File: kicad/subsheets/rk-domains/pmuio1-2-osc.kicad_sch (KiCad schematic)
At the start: 22 parts, among them U5 RK3566

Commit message: Mark as R1.0
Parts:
- renumbered C141 to C100, C142 to C101, C110 to C102, C131 to C103, C132 to C89, C133 to C90, C119 to C91, C128 to C92, C120 to C93, C139 to C94, C140 to C95, C138 to C96, C147 to C97, C143 to C98, C144 to C99, R50 to R33, R48 to R34, R49 to R35, R31 to R36, R53 to R37
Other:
- company: (none) -> UVic Rocketry

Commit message: Annotations
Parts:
- renumbered C89 to C102, C90 to C103, C91 to C104, C92 to C105, C93 to C106, C94 to C107, C95 to C108, C96 to C109, C97 to C110, C98 to C111, C99 to C112, C100 to C113, C101 to C114, C102 to C115, C103 to C116, R33 to R36, R34 to R37, R35 to R38, R36 to R39, R37 to R40

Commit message: Minor tweaks + annotations
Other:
- moved on the sheet: C102, C103

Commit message: Start on PCB design
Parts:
- C100: renamed from C102; footprint (none) -> Capacitor_SMD:C_0402_1005Metric; LCSC PART NAME (none) -> C1525
- C101: renamed from C103; footprint (none) -> Capacitor_SMD:C_0603_1608Metric; LCSC PART NAME (none) -> C15849
- C102: renamed from C104; value 18pF -> 22pF; footprint (none) -> Capacitor_SMD:C_0402_1005Metric; LCSC PART NAME (none) -> C1555
- C103: renamed from C105; footprint (none) -> Capacitor_SMD:C_0402_1005Metric; LCSC PART NAME (none) -> C1525
- C104: renamed from C106; value 18pF -> 22pF; footprint (none) -> Capacitor_SMD:C_0402_1005Metric; LCSC PART NAME (none) -> C1555
- C105: renamed from C107; footprint (none) -> Capacitor_SMD:C_0603_1608Metric; LCSC PART NAME (none) -> C15849
- C106: renamed from C108; footprint (none) -> Capacitor_SMD:C_0402_1005Metric; LCSC PART NAME (none) -> C1525
- C107: renamed from C109; footprint (none) -> Capacitor_SMD:C_0603_1608Metric; LCSC PART NAME (none) -> C15849
- C108: renamed from C110; footprint (none) -> Capacitor_SMD:C_0402_1005Metric; LCSC PART NAME (none) -> C1525
- C109: renamed from C111; footprint (none) -> Capacitor_SMD:C_0603_1608Metric; LCSC PART NAME (none) -> C15849
- C110: renamed from C112; footprint (none) -> Capacitor_SMD:C_0402_1005Metric; LCSC PART NAME (none) -> C1525
- C111: renamed from C113; footprint (none) -> Capacitor_SMD:C_0603_1608Metric; LCSC PART NAME (none) -> C15849
- C112: renamed from C114; footprint (none) -> Capacitor_SMD:C_0402_1005Metric; LCSC PART NAME (none) -> C1525
- C113: renamed from C115; footprint (none) -> Capacitor_SMD:C_0402_1005Metric; LCSC PART NAME (none) -> C1525
- C114: renamed from C116; footprint (none) -> Capacitor_SMD:C_0402_1005Metric; LCSC PART NAME (none) -> C1525
- HSE2: footprint (none) -> Crystal:Crystal_SMD_2016-4Pin_2.0x1.6mm; LCSC PART NAME (none) -> C725986
- R37: renamed from R36; footprint (none) -> Resistor_SMD:R_0402_1005Metric; LCSC PART NAME (none) -> C25092
- R38: renamed from R37; footprint (none) -> Resistor_SMD:R_0402_1005Metric; LCSC PART NAME (none) -> C17168
- R39: renamed from R38; footprint (none) -> Resistor_SMD:R_0402_1005Metric; LCSC PART NAME (none) -> C26083
- R40: renamed from R39; footprint (none) -> Resistor_SMD:R_0402_1005Metric; LCSC PART NAME (none) -> C17168
- R41: renamed from R40; footprint (none) -> Resistor_SMD:R_0402_1005Metric; LCSC PART NAME (none) -> C25076
- U5: LCSC PART NAME RK3566 -> (none)

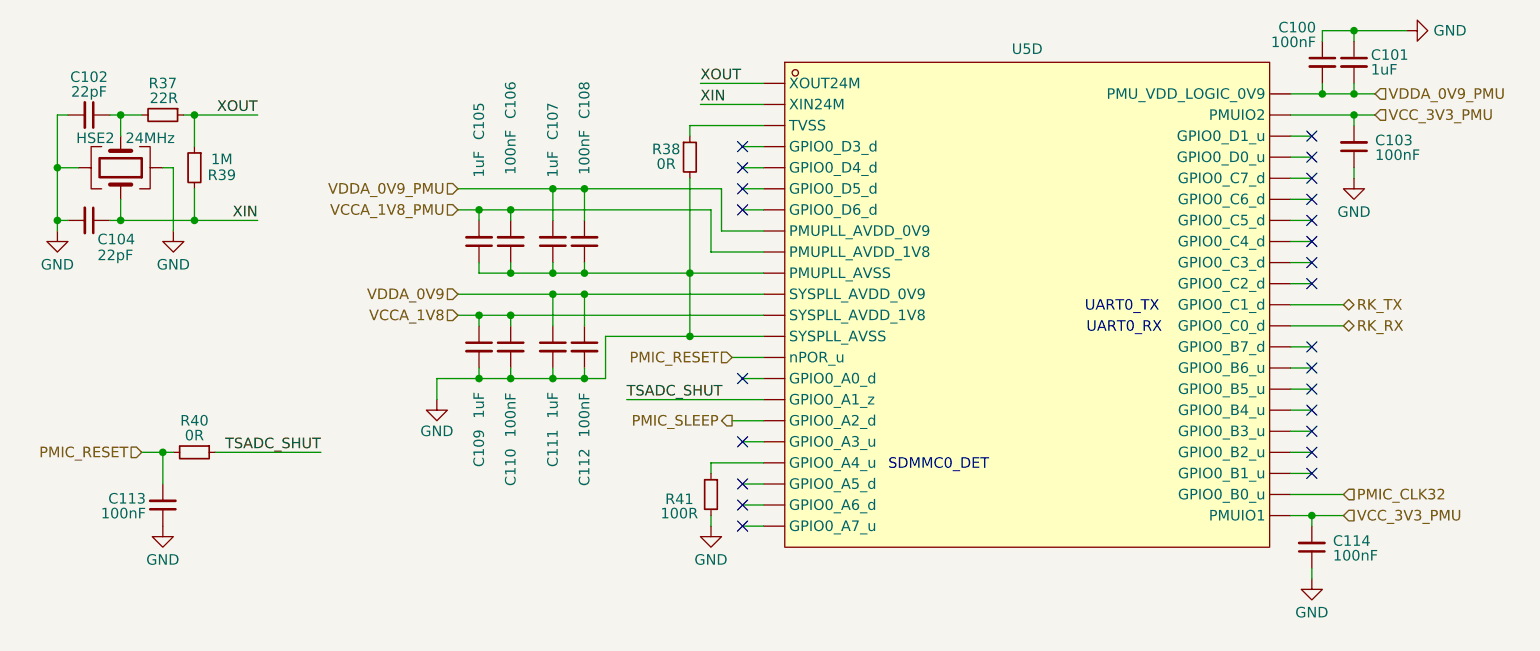
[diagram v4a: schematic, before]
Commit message: Remove power/decoupling for unused power domains
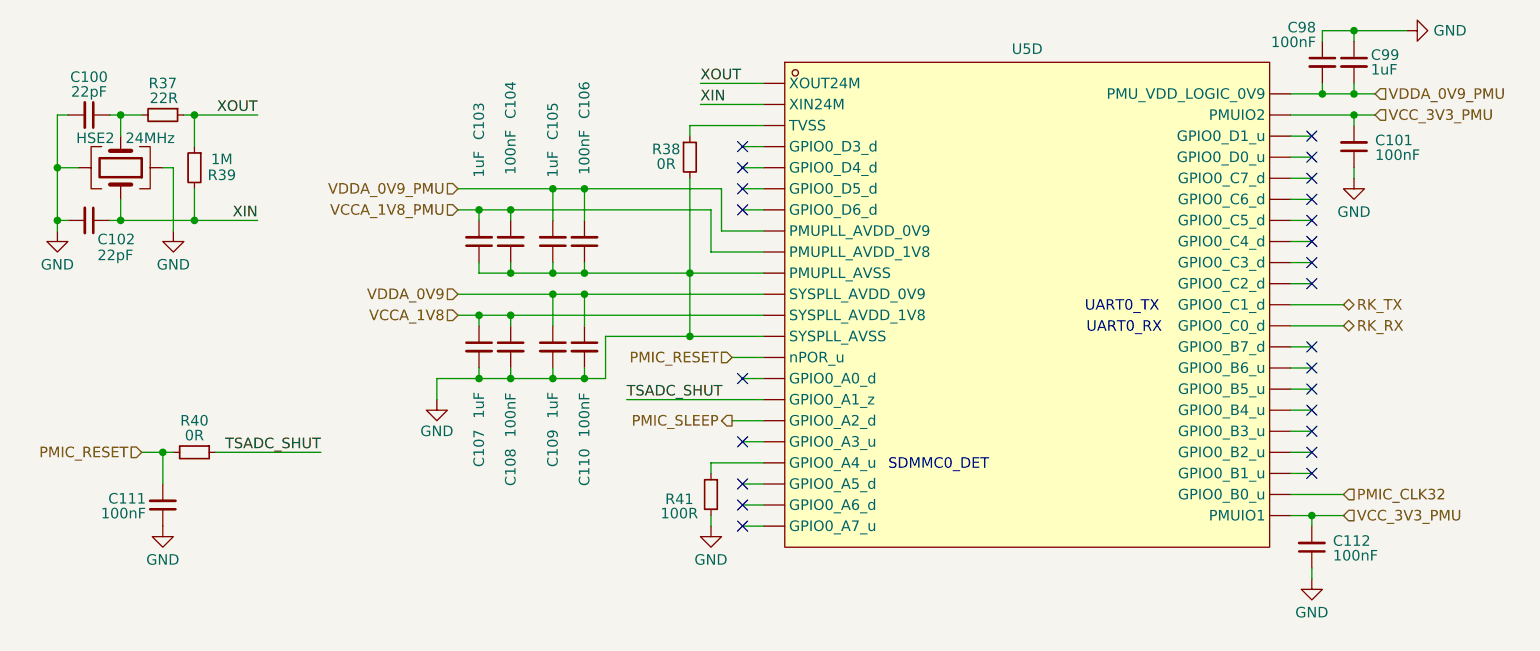
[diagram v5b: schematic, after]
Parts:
- renumbered C102 to C100, C103 to C101, C104 to C102, C105 to C103, C106 to C104, C107 to C105, C108 to C106, C109 to C107, C110 to C108, C111 to C109, C112 to C110, C113 to C111, C114 to C112, C100 to C98, C101 to C99
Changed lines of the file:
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@@
 		(on_board yes)
 		(dnp no)
-		(property "Reference" "C103"
+		(property "Reference" "C101"
 			(at 222.25 76.7145 0)
 			(effects
@@
 			(project "srad-camera"
 				(path "/da62c771-e8c9-451f-8df1-ec995aadcb11/279fc251-45a8-41a3-8fcf-5855d7fe07da/797477a3-3a48-4b27-a4d8-748eafbd5280"
-					(reference "C103")
+					(reference "C101")
 					(unit 1)
 				)
@@
 		(on_board yes)
 		(dnp no)
-		(property "Reference" "C106"
+		(property "Reference" "C104"
 			(at 118.11 69.596 90)
 			(effects
@@
 			(project "srad-camera"
 				(path "/da62c771-e8c9-451f-8df1-ec995aadcb11/279fc251-45a8-41a3-8fcf-5855d7fe07da/797477a3-3a48-4b27-a4d8-748eafbd5280"
-					(reference "C106")
+					(reference "C104")
 					(unit 1)
 				)
@@
 		(on_board yes)
 		(dnp no)
-		(property "Reference" "#PWR079"
+		(property "Reference" "#PWR082"
 			(at 142.24 129.54 0)
 			(effects
@@
 			(project "srad-camera"
 				(path "/da62c771-e8c9-451f-8df1-ec995aadcb11/279fc251-45a8-41a3-8fcf-5855d7fe07da/797477a3-3a48-4b27-a4d8-748eafbd5280"
-					(reference "#PWR079")
+					(reference "#PWR082")
 					(unit 1)
 				)
@@
 		(on_board yes)
 		(dnp no)
-		(property "Reference" "C108"
+		(property "Reference" "C106"
 			(at 127 69.596 90)
 			(effects
@@
 			(project "srad-camera"
 				(path "/da62c771-e8c9-451f-8df1-ec995aadcb11/279fc251-45a8-41a3-8fcf-5855d7fe07da/797477a3-3a48-4b27-a4d8-748eafbd5280"
-					(reference "C108")
+					(reference "C106")
 					(unit 1)
 				)
@@
 		(on_board yes)
 		(dnp no)
-		(property "Reference" "C114"
+		(property "Reference" "C112"
 			(at 217.17 124.9745 0)
 			(effects
@@
 			(project "srad-camera"
 				(path "/da62c771-e8c9-451f-8df1-ec995aadcb11/279fc251-45a8-41a3-8fcf-5855d7fe07da/797477a3-3a48-4b27-a4d8-748eafbd5280"
-					(reference "C114")
+					(reference "C112")
 					(unit 1)
 				)
@@
 		(on_board yes)
 		(dnp no)
-		(property "Reference" "#PWR076"
+		(property "Reference" "#PWR079"
 			(at 77.47 93.98 0)
 			(effects
@@
 			(project "srad-camera"
 				(path "/da62c771-e8c9-451f-8df1-ec995aadcb11/279fc251-45a8-41a3-8fcf-5855d7fe07da/797477a3-3a48-4b27-a4d8-748eafbd5280"
-					(reference "#PWR076")
+					(reference "#PWR079")
 					(unit 1)
 				)
@@
 		(on_board yes)
 		(dnp no)
-		(property "Reference" "C101"
+		(property "Reference" "C99"
 			(at 221.742 66.4275 0)
 			(effects
@@
 			(project "srad-camera"
 				(path "/da62c771-e8c9-451f-8df1-ec995aadcb11/279fc251-45a8-41a3-8fcf-5855d7fe07da/797477a3-3a48-4b27-a4d8-748eafbd5280"
-					(reference "C101")
+					(reference "C99")
 					(unit 1)
 				)
@@
 		(on_board yes)
 		(dnp no)
-		(property "Reference" "C112"
+		(property "Reference" "C110"
 			(at 127 118.364 90)
 			(effects
@@
 			(project "srad-camera"
 				(path "/da62c771-e8c9-451f-8df1-ec995aadcb11/279fc251-45a8-41a3-8fcf-5855d7fe07da/797477a3-3a48-4b27-a4d8-748eafbd5280"
-					(reference "C112")
+					(reference "C110")
 					(unit 1)
 				)
@@
 		(on_board yes)
 		(dnp no)
-		(property "Reference" "#PWR077"
+		(property "Reference" "#PWR080"
 			(at 109.22 114.3 0)
 			(effects
@@
 			(project "srad-camera"
 				(path "/da62c771-e8c9-451f-8df1-ec995aadcb11/279fc251-45a8-41a3-8fcf-5855d7fe07da/797477a3-3a48-4b27-a4d8-748eafbd5280"
-					(reference "#PWR077")
+					(reference "#PWR080")
 					(unit 1)
 				)
@@
 		(on_board yes)
 		(dnp no)
-		(property "Reference" "C107"
+		(property "Reference" "C105"
 			(at 123.19 72.136 90)
 			(effects
@@
 			(project "srad-camera"
 				(path "/da62c771-e8c9-451f-8df1-ec995aadcb11/279fc251-45a8-41a3-8fcf-5855d7fe07da/797477a3-3a48-4b27-a4d8-748eafbd5280"
-					(reference "C107")
+					(reference "C105")
 					(unit 1)
 				)
@@
 		(on_board yes)
 		(dnp no)
-		(property "Reference" "#PWR075"
+		(property "Reference" "#PWR078"
 			(at 63.5 93.98 0)
 			(effects
@@
 			(project "srad-camera"
 				(path "/da62c771-e8c9-451f-8df1-ec995aadcb11/279fc251-45a8-41a3-8fcf-5855d7fe07da/797477a3-3a48-4b27-a4d8-748eafbd5280"
-					(reference "#PWR075")
+					(reference "#PWR078")
 					(unit 1)
 				)
@@
 		(on_board yes)
 		(dnp no)
-		(property "Reference" "C100"
+		(property "Reference" "C98"
 			(at 215.138 63.119 0)
 			(effects
@@
 			(project "srad-camera"
 				(path "/da62c771-e8c9-451f-8df1-ec995aadcb11/279fc251-45a8-41a3-8fcf-5855d7fe07da/797477a3-3a48-4b27-a4d8-748eafbd5280"
-					(reference "C100")
+					(reference "C98")
 					(unit 1)
 				)
@@
 		(dnp no)
 		(fields_autoplaced yes)
-		(property "Reference" "#PWR080"
+		(property "Reference" "#PWR083"
 			(at 214.63 135.89 0)
 			(effects
@@
 			(project "srad-camera"
 				(path "/da62c771-e8c9-451f-8df1-ec995aadcb11/279fc251-45a8-41a3-8fcf-5855d7fe07da/797477a3-3a48-4b27-a4d8-748eafbd5280"
-					(reference "#PWR080")
+					(reference "#PWR083")
 					(unit 1)
 				)
@@
 		(dnp no)
 		(fields_autoplaced yes)
-		(property "Reference" "#PWR074"
+		(property "Reference" "#PWR077"
 			(at 219.71 87.63 0)
 			(effects
@@
 			(project "srad-camera"
 				(path "/da62c771-e8c9-451f-8df1-ec995aadcb11/279fc251-45a8-41a3-8fcf-5855d7fe07da/797477a3-3a48-4b27-a4d8-748eafbd5280"
-					(reference "#PWR074")
+					(reference "#PWR077")
 					(unit 1)
 				)
@@
 		(on_board yes)
 		(dnp no)
-		(property "Reference" "C105"
+		(property "Reference" "C103"
 			(at 114.3 72.136 90)
 			(effects
@@
 			(project "srad-camera"
 				(path "/da62c771-e8c9-451f-8df1-ec995aadcb11/279fc251-45a8-41a3-8fcf-5855d7fe07da/797477a3-3a48-4b27-a4d8-748eafbd5280"
-					(reference "C105")
+					(reference "C103")
 					(unit 1)
 				)
@@
 		(on_board yes)
 		(dnp no)
-		(property "Reference" "C104"
+		(property "Reference" "C102"
 			(at 68.326 88.646 90)
 			(effects
@@
 			(project "srad-camera"
 				(path "/da62c771-e8c9-451f-8df1-ec995aadcb11/279fc251-45a8-41a3-8fcf-5855d7fe07da/797477a3-3a48-4b27-a4d8-748eafbd5280"
-					(reference "C104")
+					(reference "C102")
 					(unit 1)
 				)
@@
 		(on_board yes)
 		(dnp no)
-		(property "Reference" "C110"
+		(property "Reference" "C108"
 			(at 118.11 118.364 90)
 			(effects
@@
 			(project "srad-camera"
 				(path "/da62c771-e8c9-451f-8df1-ec995aadcb11/279fc251-45a8-41a3-8fcf-5855d7fe07da/797477a3-3a48-4b27-a4d8-748eafbd5280"
-					(reference "C110")
+					(reference "C108")
 					(unit 1)
 				)
@@
 		(on_board yes)
 		(dnp no)
-		(property "Reference" "C113"
+		(property "Reference" "C111"
 			(at 74.168 119.888 0)
 			(effects
@@
 			(project "srad-camera"
 				(path "/da62c771-e8c9-451f-8df1-ec995aadcb11/279fc251-45a8-41a3-8fcf-5855d7fe07da/797477a3-3a48-4b27-a4d8-748eafbd5280"
-					(reference "C113")
+					(reference "C111")
 					(unit 1)
 				)
@@
 		(on_board yes)
 		(dnp no)
-		(property "Reference" "C109"
+		(property "Reference" "C107"
 			(at 114.3 116.078 90)
 			(effects
@@
 			(project "srad-camera"
 				(path "/da62c771-e8c9-451f-8df1-ec995aadcb11/279fc251-45a8-41a3-8fcf-5855d7fe07da/797477a3-3a48-4b27-a4d8-748eafbd5280"
-					(reference "C109")
+					(reference "C107")
 					(unit 1)
 				)
@@
 		(on_board yes)
 		(dnp no)
-		(property "Reference" "C102"
+		(property "Reference" "C100"
 			(at 67.31 69.088 90)
 			(effects
@@
 			(project "srad-camera"
 				(path "/da62c771-e8c9-451f-8df1-ec995aadcb11/279fc251-45a8-41a3-8fcf-5855d7fe07da/797477a3-3a48-4b27-a4d8-748eafbd5280"
-					(reference "C102")
+					(reference "C100")
 					(unit 1)
 				)
@@
 		(dnp no)
 		(fields_autoplaced yes)
-		(property "Reference" "#PWR073"
+		(property "Reference" "#PWR076"
 			(at 232.41 63.5 0)
 			(effects
@@
 			(project "srad-camera"
 				(path "/da62c771-e8c9-451f-8df1-ec995aadcb11/279fc251-45a8-41a3-8fcf-5855d7fe07da/797477a3-3a48-4b27-a4d8-748eafbd5280"
-					(reference "#PWR073")
+					(reference "#PWR076")
 					(unit 1)
 				)
@@
 		(on_board yes)
 		(dnp no)
-		(property "Reference" "C111"
+		(property "Reference" "C109"
 			(at 123.19 116.078 90)
 			(effects
@@
 			(project "srad-camera"
 				(path "/da62c771-e8c9-451f-8df1-ec995aadcb11/279fc251-45a8-41a3-8fcf-5855d7fe07da/797477a3-3a48-4b27-a4d8-748eafbd5280"
-					(reference "C111")
+					(reference "C109")
 					(unit 1)
 				)
@@
 		(dnp no)
 		(fields_autoplaced yes)
-		(property "Reference" "#PWR078"
+		(property "Reference" "#PWR081"
 			(at 76.2 129.54 0)
 			(effects
@@
 			(project "srad-camera"
 				(path "/da62c771-e8c9-451f-8df1-ec995aadcb11/279fc251-45a8-41a3-8fcf-5855d7fe07da/797477a3-3a48-4b27-a4d8-748eafbd5280"
-					(reference "#PWR078")
+					(reference "#PWR081")
 					(unit 1)
 				)

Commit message: PCB done besides fixing screwups + length matching
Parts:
- removed R38, R40: 0R, Resistor_SMD:R_0402_1005Metric, symbol Device:R_Small
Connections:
- net TSADC_SHUT is gone; now on net PMIC_RESET: U5.1R20 (GPIO0_A1_z)
- net GND: now also U5.1M18 (TVSS)
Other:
- moved on the sheet: C111
